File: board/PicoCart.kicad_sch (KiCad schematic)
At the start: 29 parts, among them J1 MSX Bus (Odd-Even), J2 Micro_SD_Card, J3 UART, J4 DEBUG, J5 MSX Debug, J6 Pico Debug, J7 Ground Pins, J8 Ground Pins, J9 Edge Connector, U1 LD1117S33TR_SOT223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

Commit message: Tidied up Schematic
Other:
- company: (none) -> NormStudios
- title: (none) -> PicoCart
- moved on the sheet: C1, C10, C11, C2, C3, C4, C5, C6, C7, C8, C9, J1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

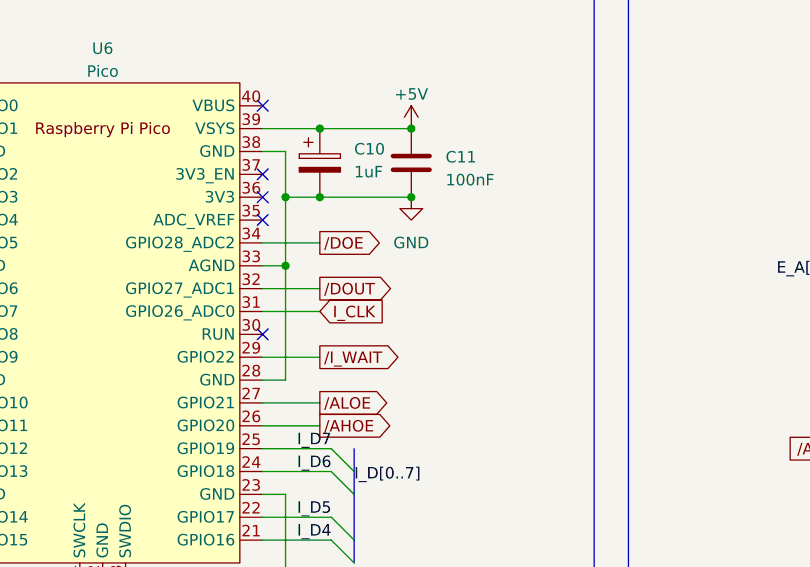
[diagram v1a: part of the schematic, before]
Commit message: Swapped DoE and IWait
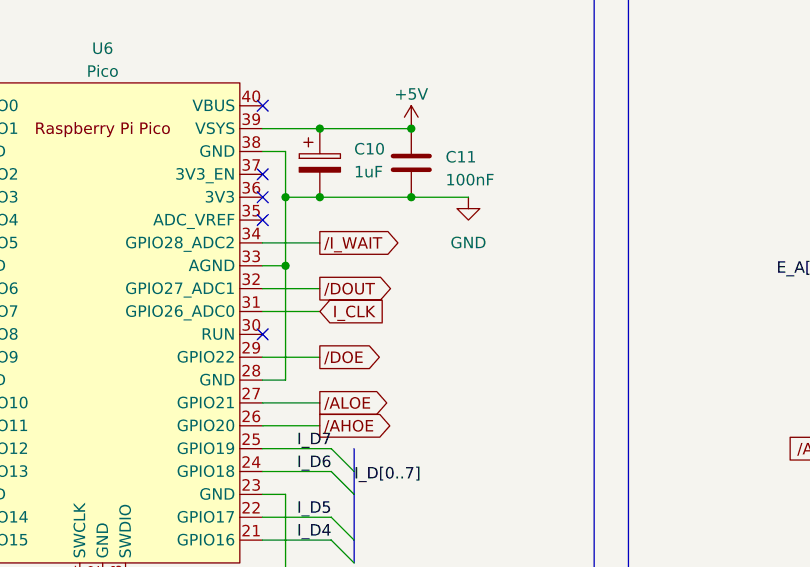
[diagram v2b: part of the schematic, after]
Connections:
- net /DOE: now also U6.29 (GPIO22); no longer U6.34 (GPIO28_ADC2)
- net /I_WAIT: now also U6.34 (GPIO28_ADC2); no longer U6.29 (GPIO22)
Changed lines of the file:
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@@
+    (stroke (width 0) (type default))
+  )
+  (wire (pts (xy 102.87 66.04) (xy 96.52 66.04))
     (stroke (width 0) (type default))
   )
@@
     )
   )
+  (global_label "{slash}DOE" (shape output) (at 86.36 83.82 0) (fields_autoplaced)
+    (effects (font (size 1.27 1.27)) (justify left))
+    (property "Intersheetrefs" "${INTERSHEET_REFS}" (at 94.3458 83.82 0)
+      (effects (font (size 1.27 1.27)) (justify left) hide)
+    )
+  )
   (global_label "{slash}DOUT" (shape input) (at 146.05 204.47 180) (fields_autoplaced)
     (effects (font (size 1.27 1.27)) (justify right))
@@
     )
   )
-  (global_label "{slash}I_WAIT" (shape output) (at 86.36 83.82 0) (fields_autoplaced)
-    (effects (font (size 1.27 1.27)) (justify left))
-    (property "Intersheetrefs" "${INTERSHEET_REFS}" (at 96.2811 83.82 0)
-      (effects (font (size 1.27 1.27)) (justify left) hide)
-    )
-  )
   (global_label "{slash}WAIT" (shape input) (at 240.03 54.61 180) (fields_autoplaced)
     (effects (font (size 1.27 1.27)) (justify right))
@@
     )
   )
-  (global_label "{slash}DOE" (shape output) (at 86.36 71.12 0) (fields_autoplaced)
-    (effects (font (size 1.27 1.27)) (justify left))
-    (property "Intersheetrefs" "${INTERSHEET_REFS}" (at 94.3458 71.12 0)
-      (effects (font (size 1.27 1.27)) (justify left) hide)
-    )
-  )
   (global_label "{slash}E_READ" (shape output) (at 273.05 62.23 0) (fields_autoplaced)
     (effects (font (size 1.27 1.27)) (justify left))
@@
     (effects (font (size 1.27 1.27)) (justify left))
     (property "Intersheetrefs" "${INTERSHEET_REFS}" (at 285.0877 191.77 0)
+      (effects (font (size 1.27 1.27)) (justify left) hide)
+    )
+  )
+  (global_label "{slash}I_WAIT" (shape output) (at 86.36 71.12 0) (fields_autoplaced)
+    (effects (font (size 1.27 1.27)) (justify left))
+    (property "Intersheetrefs" "${INTERSHEET_REFS}" (at 96.2811 71.12 0)
       (effects (font (size 1.27 1.27)) (justify left) hide)
     )
@@
     )
   )
-  (symbol (lib_id "power:GND") (at 96.52 66.04 0) (unit 1)
+  (symbol (lib_id "power:GND") (at 102.87 66.04 0) (unit 1)
     (in_bom yes) (on_board yes) (dnp no) (fields_autoplaced)
-    (property "Reference" "#PWR036" (at 96.52 72.39 0)
-      (effects (font (size 1.27 1.27)) hide)
-    )
-    (property "Value" "GND" (at 96.52 71.12 0)
+    (property "Reference" "#PWR036" (at 102.87 72.39 0)
+      (effects (font (size 1.27 1.27)) hide)
+    )
+    (property "Value" "GND" (at 102.87 71.12 0)
       (effects (font (size 1.27 1.27)))
     )
-    (property "Footprint" "" (at 96.52 66.04 0)
-      (effects (font (size 1.27 1.27)) hide)
-    )
-    (property "Datasheet" "" (at 96.52 66.04 0)
-      (effects (font (size 1.27 1.27)) hide)
-    )
+    (property "Footprint" "" (at 102.87 66.04 0)
+      (effects (font (size 1.27 1.27)) hide)
+    )
+    (property "Datasheet" "" (at 102.87 66.04 0)
+      (effects (font (size 1.27 1.27)) hide)
+    )
